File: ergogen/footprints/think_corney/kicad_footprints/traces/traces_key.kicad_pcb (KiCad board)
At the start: 2 copper layers, 4 parts

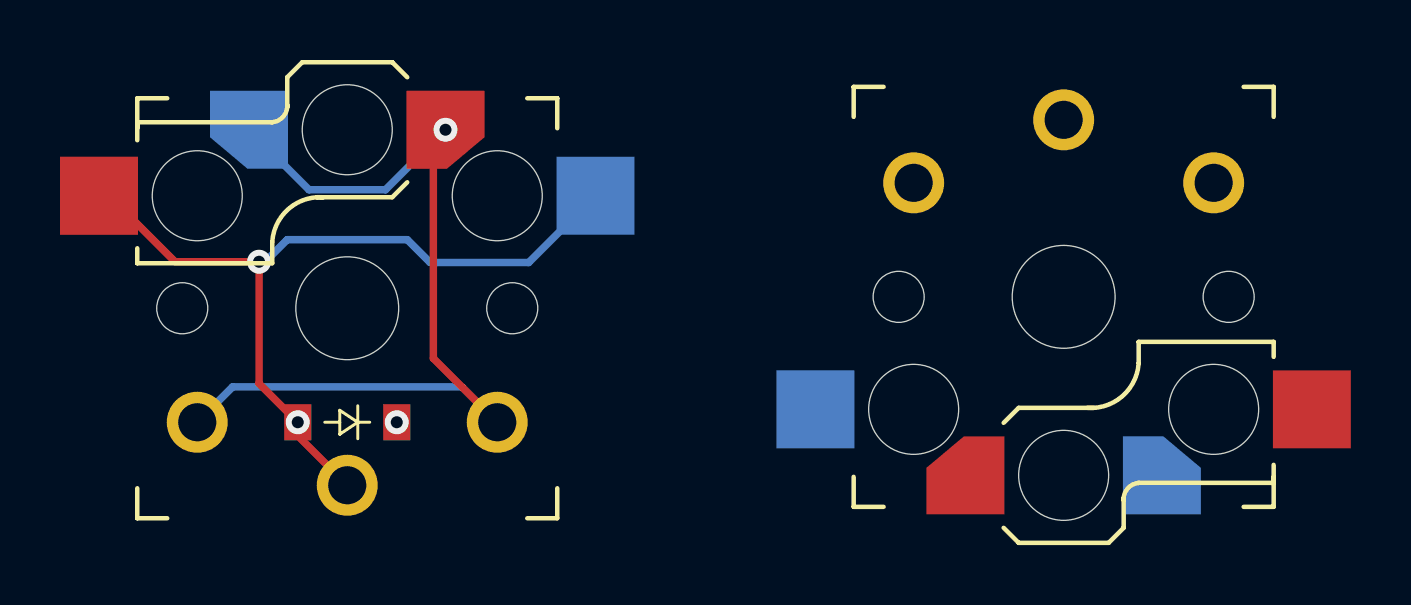
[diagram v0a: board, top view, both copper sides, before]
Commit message: Key Traces: Fix too long traces when using smaller hotswap pads
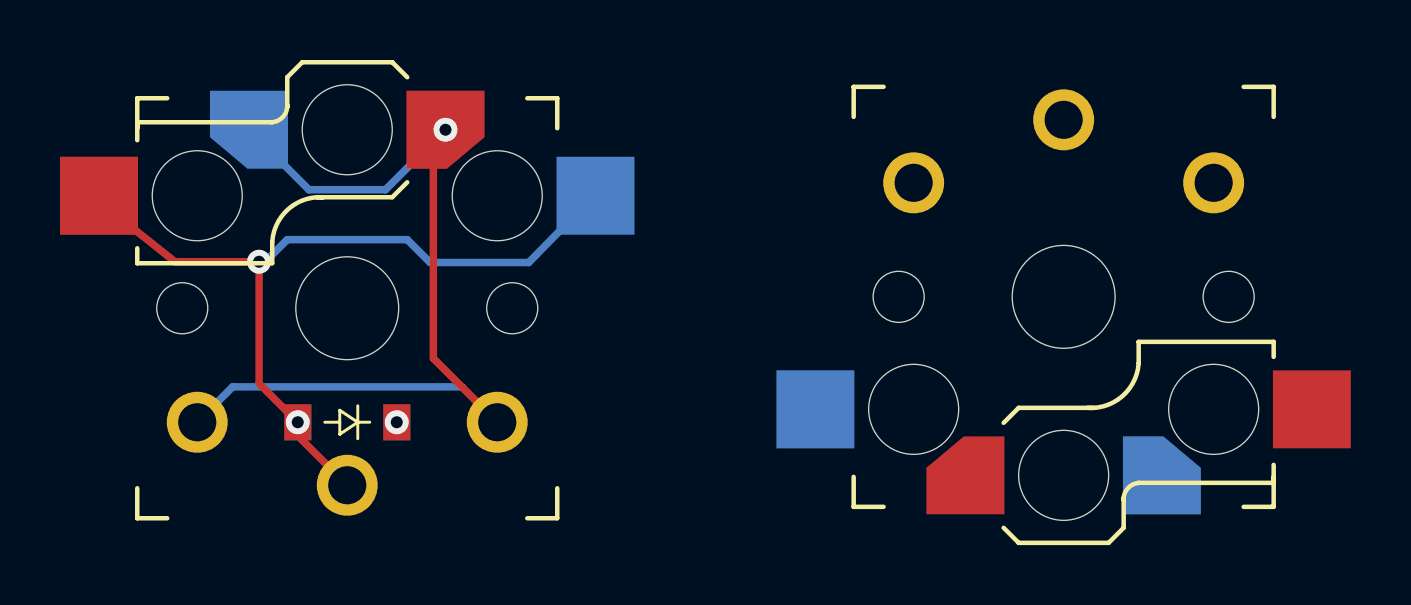
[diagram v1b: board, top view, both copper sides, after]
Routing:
- net middle_home: track 27.7 -> 24.7 mm
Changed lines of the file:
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@@
   (segment (start -5.74 -1.55) (end -2.94 -1.55) (width 0.25) (layer "F.Cu") (net 3))
   (segment (start -1.65 3.8) (end -1.65 4.25) (width 0.25) (layer "F.Cu") (net 3))
-  (segment (start -8.275 -3.75) (end -7.94 -3.75) (width 0.25) (layer "F.Cu") (net 3))
-  (segment (start -7.94 -3.75) (end -5.74 -1.55) (width 0.25) (layer "F.Cu") (net 3))
+  (segment (start -7.25 -2.75) (end -5.74 -1.55) (width 0.25) (layer "F.Cu") (net 3))
   (segment (start -2.94 -1.55) (end -2.94 2.51) (width 0.25) (layer "F.Cu") (net 3))
   (segment (start -2.94 2.51) (end -1.65 3.8) (width 0.25) (layer "F.Cu") (net 3))
@@
   (segment (start 6.049 -1.524) (end 2.762 -1.524) (width 0.25) (layer "B.Cu") (net 3))
   (segment (start 2.762 -1.524) (end 2 -2.286) (width 0.25) (layer "B.Cu") (net 3))
-  (segment (start 8.275 -3.75) (end 6.049 -1.524) (width 0.25) (layer "B.Cu") (net 3))
+  (segment (start 7.25 -2.75) (end 6.049 -1.524) (width 0.25) (layer "B.Cu") (net 3))
 )
